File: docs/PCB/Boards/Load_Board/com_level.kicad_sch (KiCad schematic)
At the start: 38 parts, among them J10 Conn_01x02_Pin, J11 Conn_01x02_Pin, J12 Conn_01x02_Pin, J13 Conn_01x02_Pin, J14 Conn_01x02_Pin, J15 Conn_01x02_Pin, J16 Conn_01x02_Pin, J3 Conn_01x06_Pin, J4 Conn_01x06_Pin, J5 Conn_01x02_Pin, J6 Conn_01x02_Pin, J7 Conn_01x02_Pin, J8 Conn_01x02_Pin, J9 Conn_01x02_Pin, Q1 BSS138, Q2 BSS138, Q3 BSS138, Q4 BSS138, Q5 BSS138, Q6 BSS138

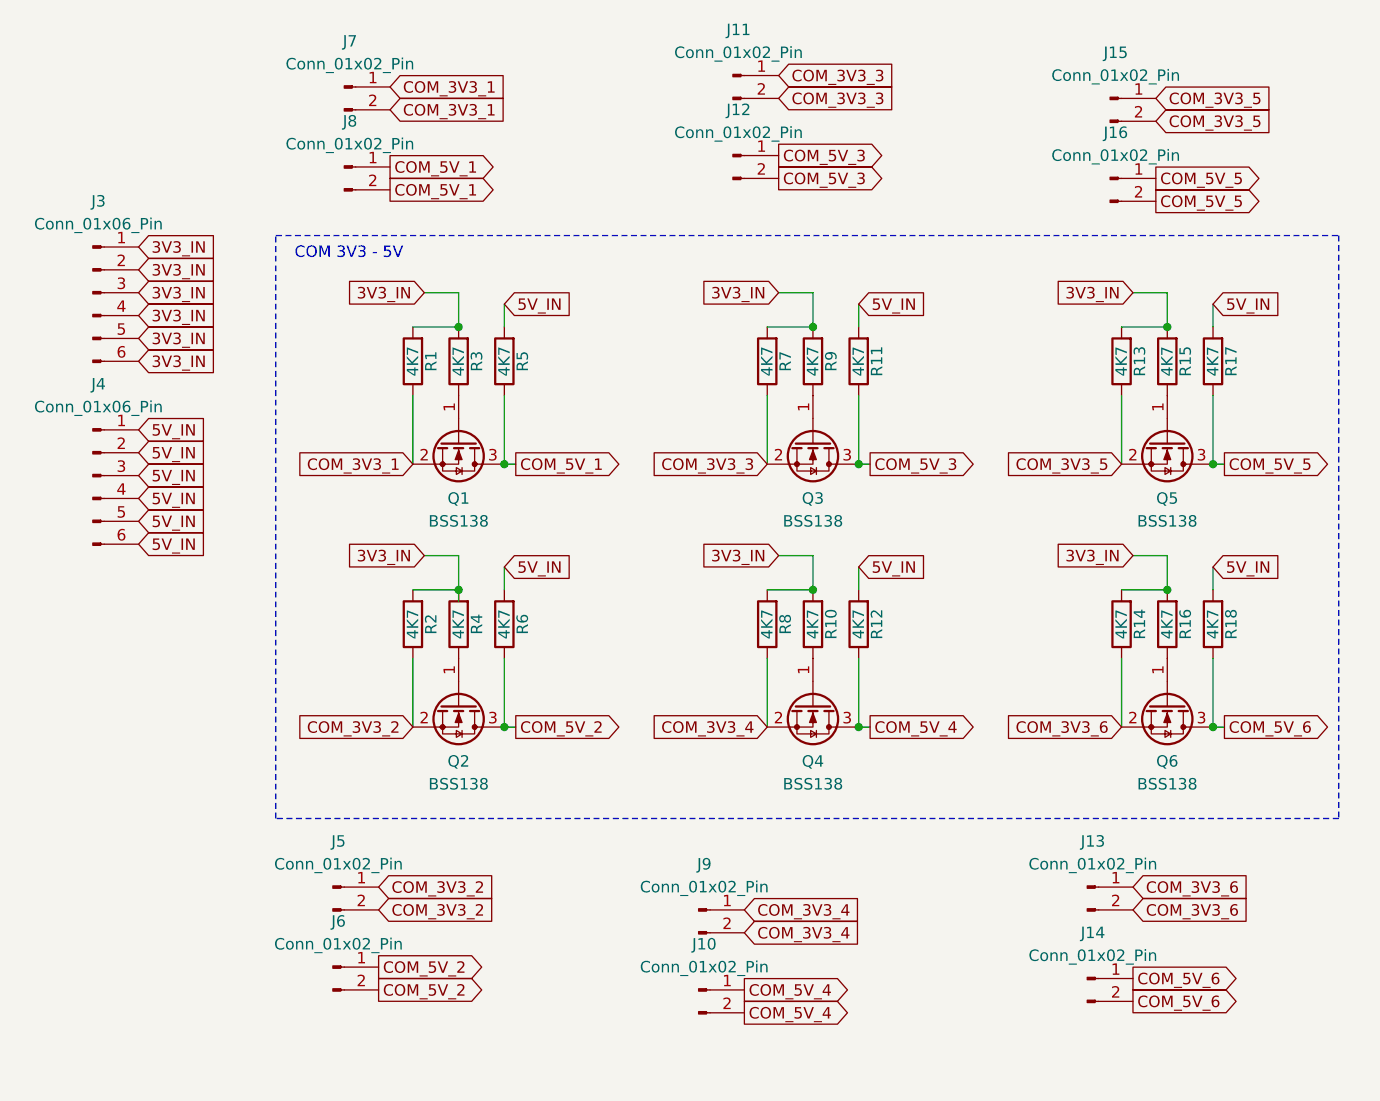
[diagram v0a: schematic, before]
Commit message: Load board and ATMega Board added
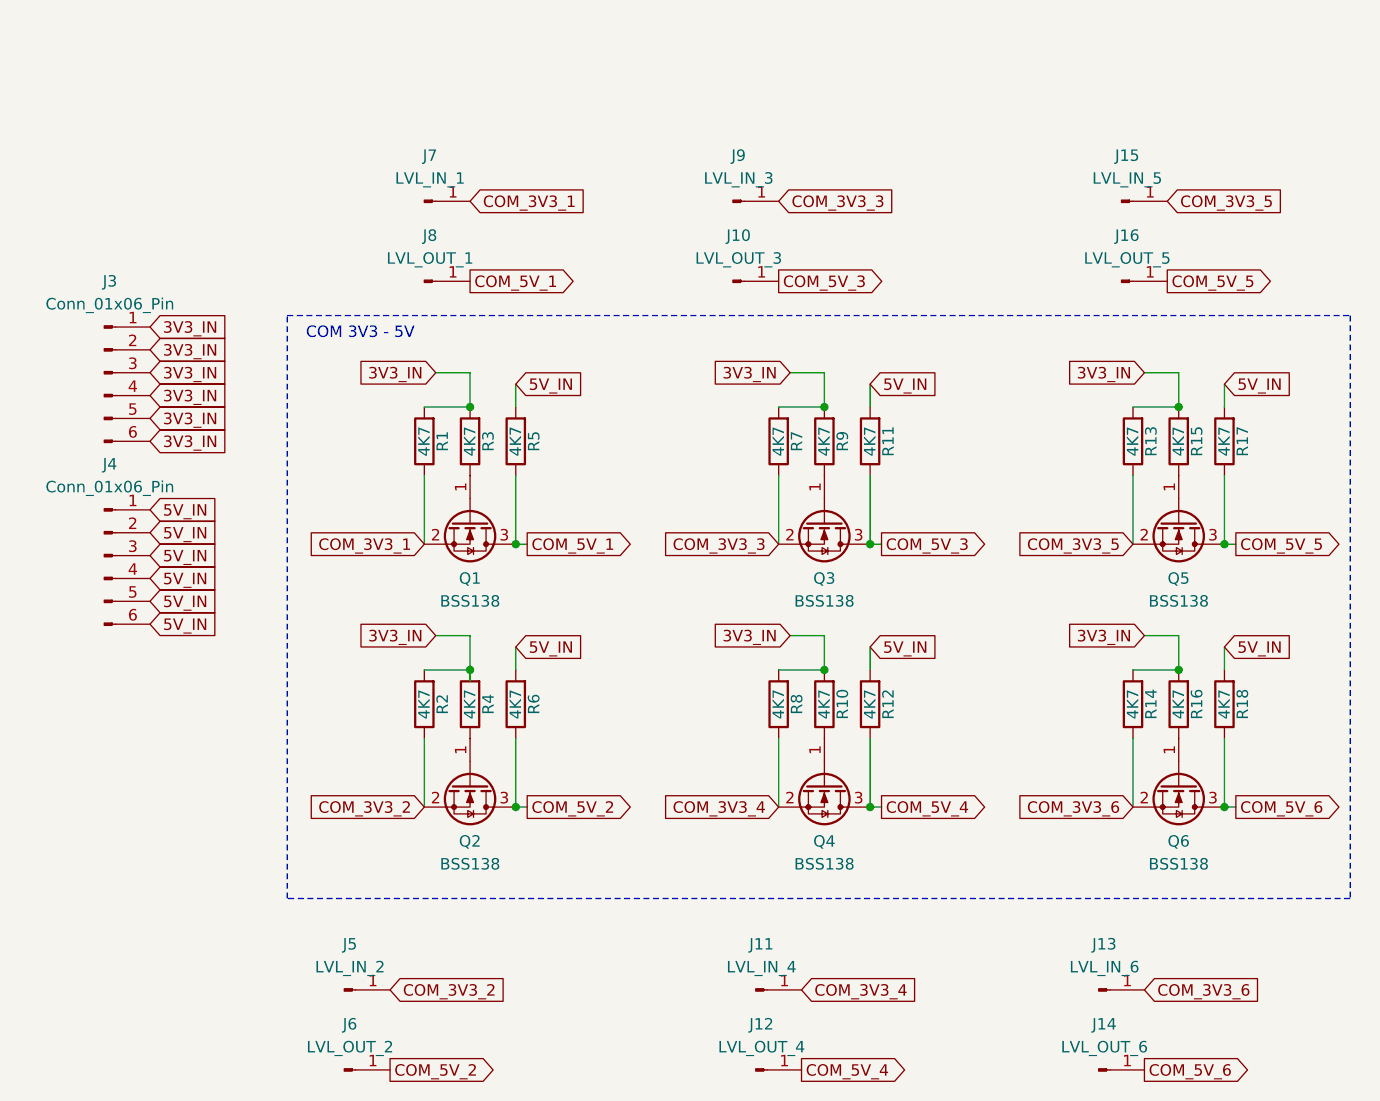
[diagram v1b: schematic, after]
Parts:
- removed J10, J11, J12, J13, J14, J15, J16, J5, J6, J7, J8, J9: Conn_01x02_Pin, Connector_PinHeader_2.54mm:PinHeader_1x02_P2.54mm_Vertical, symbol Connector:Conn_01x02_Pin
- added J10: LVL_OUT_3, Connector_PinHeader_2.54mm:PinHeader_1x01_P2.54mm_Vertical, symbol Connector:Conn_01x01_Pin
- added J11: LVL_IN_4, Connector_PinHeader_2.54mm:PinHeader_1x01_P2.54mm_Vertical, symbol Connector:Conn_01x01_Pin
- added J12: LVL_OUT_4, Connector_PinHeader_2.54mm:PinHeader_1x01_P2.54mm_Vertical, symbol Connector:Conn_01x01_Pin
- added J13: LVL_IN_6, Connector_PinHeader_2.54mm:PinHeader_1x01_P2.54mm_Vertical, symbol Connector:Conn_01x01_Pin
- added J14: LVL_OUT_6, Connector_PinHeader_2.54mm:PinHeader_1x01_P2.54mm_Vertical, symbol Connector:Conn_01x01_Pin
- added J15: LVL_IN_5, Connector_PinHeader_2.54mm:PinHeader_1x01_P2.54mm_Vertical, symbol Connector:Conn_01x01_Pin
- added J16: LVL_OUT_5, Connector_PinHeader_2.54mm:PinHeader_1x01_P2.54mm_Vertical, symbol Connector:Conn_01x01_Pin
- added J5: LVL_IN_2, Connector_PinHeader_2.54mm:PinHeader_1x01_P2.54mm_Vertical, symbol Connector:Conn_01x01_Pin
- added J6: LVL_OUT_2, Connector_PinHeader_2.54mm:PinHeader_1x01_P2.54mm_Vertical, symbol Connector:Conn_01x01_Pin
- added J7: LVL_IN_1, Connector_PinHeader_2.54mm:PinHeader_1x01_P2.54mm_Vertical, symbol Connector:Conn_01x01_Pin
- added J8: LVL_OUT_1, Connector_PinHeader_2.54mm:PinHeader_1x01_P2.54mm_Vertical, symbol Connector:Conn_01x01_Pin
- added J9: LVL_IN_3, Connector_PinHeader_2.54mm:PinHeader_1x01_P2.54mm_Vertical, symbol Connector:Conn_01x01_Pin
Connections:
- net COM_3V3_1: now also J7.1 (Pin_1)
- net COM_3V3_2: now also J5.1 (Pin_1)
- net COM_3V3_3: now also J9.1 (Pin_1)
- net COM_3V3_4: now also J11.1 (Pin_1)
- net COM_3V3_5: now also J15.1 (Pin_1)
- net COM_3V3_6: now also J13.1 (Pin_1)
- net COM_5V_1: now also J8.1 (Pin_1)
- net COM_5V_2: now also J6.1 (Pin_1)
- net COM_5V_3: now also J10.1 (Pin_1)
- net COM_5V_4: now also J12.1 (Pin_1)
- net COM_5V_5: now also J16.1 (Pin_1)
- net COM_5V_6: now also J14.1 (Pin_1)
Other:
- company: (none) -> PKl
- title: (none) -> COM_Level
- moved on the sheet: J3, J4, Q1, Q2, Q3, Q4, Q5, Q6, R1, R10, R11, R12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
